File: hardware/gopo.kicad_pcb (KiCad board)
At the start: 4 copper layers, 65.9 x 40.6 mm, 99 parts, among them J2 DS1021-1X3SF11-B, J3 NHD-2.4-240320AF-CSXP, J4 DG142R-5.08-02P-14-00AH, J7 USB_C_Receptacle_USB2.0_16P, Q1 BSS138, Q2 BSS138, Q3 IRF7855TRPBF, Q4 IRF7855TRPBF, SW1 BOOT / PTS810, SW2 RESET / PTS810, SW3 L-KLS4-EC1121S-E5A-F12.5, U1 AP33772SDKZ-13-FA02, U10 TPD4EUSB30, U2 ESP32-C6-WROOM-1, U3 INA228, U4 RV-3028-C7, U5 AOZ1284PI, U6 TL431BIDBZR, U7 TPS61023DRLR, U8 CAT4104V-GT3, U9 TPD4E05U06QDQARQ1

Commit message: hardware: RTC'yi BQ32000 + süper kapasitöre geçir, Özdisan BOM'unu şemaya aktar
RTC (mcu):
- U4 RV-3028-C7 -> BQ32000DR (SOIC-8, I2C 0x68, open-drain IRQ, dahili
  trickle charger). Y1 ABS25-32.768KHZ-T (CL 12,5 pF, harici yük C yok),
  C33 Korchip DCL5R5155HF 1,5 F/5,5 V (H-tipi yatay coin, ~22 gün yedek).
- BT1 (CR2032), R22, R23, C10 kaldırıldı; C9 100n -> 1u0 (datasheet >= 1 uF).
- Yeni footprint: Power_Output_Custom:Korchip_DCL_H-Type_D19.0mm_P20.00mm_Horizontal
  (Korchip DCL datasheet çiziminden; numune ile doğrulanmalı).
- Beklenen netlist farkı yalnız RTC netleri: RTC_SCL/SDA/INT U4 pin
  numaraları, Net-(U4-OSCI/OSCO/VBACK) yeni; Net-(BT1-+), Net-(U4-EVI),
  Net-(U4-VBACKUP), U4 CLKOUT kalktı. ERC değişmedi (0 hata, 2 eski uyarı).

Özdisan BOM aktarımı (tüm sayfalar):
- MPN, Manufacturer, parametrik alanlar ve SelectionNote (Özdisan kodu,
  stok 21.09.2026, durum) BOM_OZDISAN_REV_C_20260921.xlsx'ten yazıldı.
- Onaylı değişiklikler: C5/C20/C21 0805; C8/C12/C13/C25/C27/C28 4u7 50V
  X7R 1210; C15/C29 47u 35V hibrit (Device:C_Polarized, CP_Elec_6.3x5.8);
  C31 0603 25V; R59 0805 1/3W; R40 3k24 + R39 10k2 (VOUT 3,3185 V);
  U6 TL431AIDBZR; D4 SX36.
- Stokta olmayan parçalarda (U1, U2, U7, U8, U10, U12, L1, L2, C19) MPN
  korundu, öneri SelectionNote ve todo.txt'de. Alan geometrisi ve
  görünürlük değişmedi. PCB şemadan henüz güncellenmedi.

Aynı commit'te önceden commit edilmemiş çalışma: Q3/Q5 SQJB60EP ve U3
INA226 entegrasyonu, raporları ve datasheet'leri.

Co-Authored-By: Claude Opus 5 <noreply@anthropic.com>
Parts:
- U3: value INA228 -> INA226
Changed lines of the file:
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@@
 			)
 		)
-		(property "Value" "INA228"
+		(property "Value" "INA226"
 			(at 0 -2.45 90)
 			(layer "B.Fab")
@@
 			)
 		)
-		(property "MPN" "INA228AIDGSR"
+		(property "MPN" "INA226AIDGSR"
 			(at 0 0 270)
 			(unlocked yes)

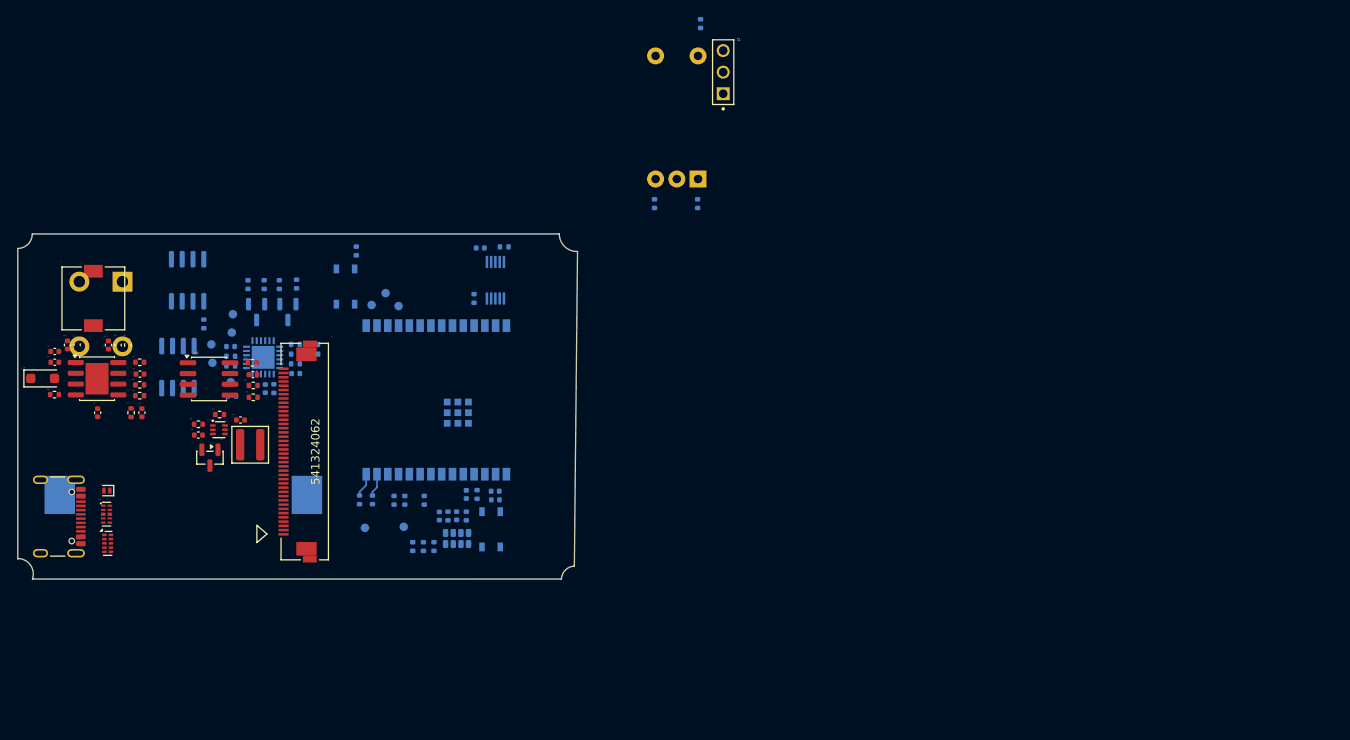
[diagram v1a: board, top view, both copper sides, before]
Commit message: hardware: PCB'yi şemadan güncelle (TASK-006)
54 footprint eklendi, 15 kaldırıldı, 20 footprint değişti; alanlar ve
netler şemayla eşitlendi, eski WROOM-1/BT1 pad'lerine giden 7 iz
parçası silindi. DRC schematic parity 416 -> 1 (J8, footprint TBD).
kicad-schematic skill'ine headless update_pcb.py eklendi.

Co-Authored-By: Claude Opus 5.5 <noreply@anthropic.com>
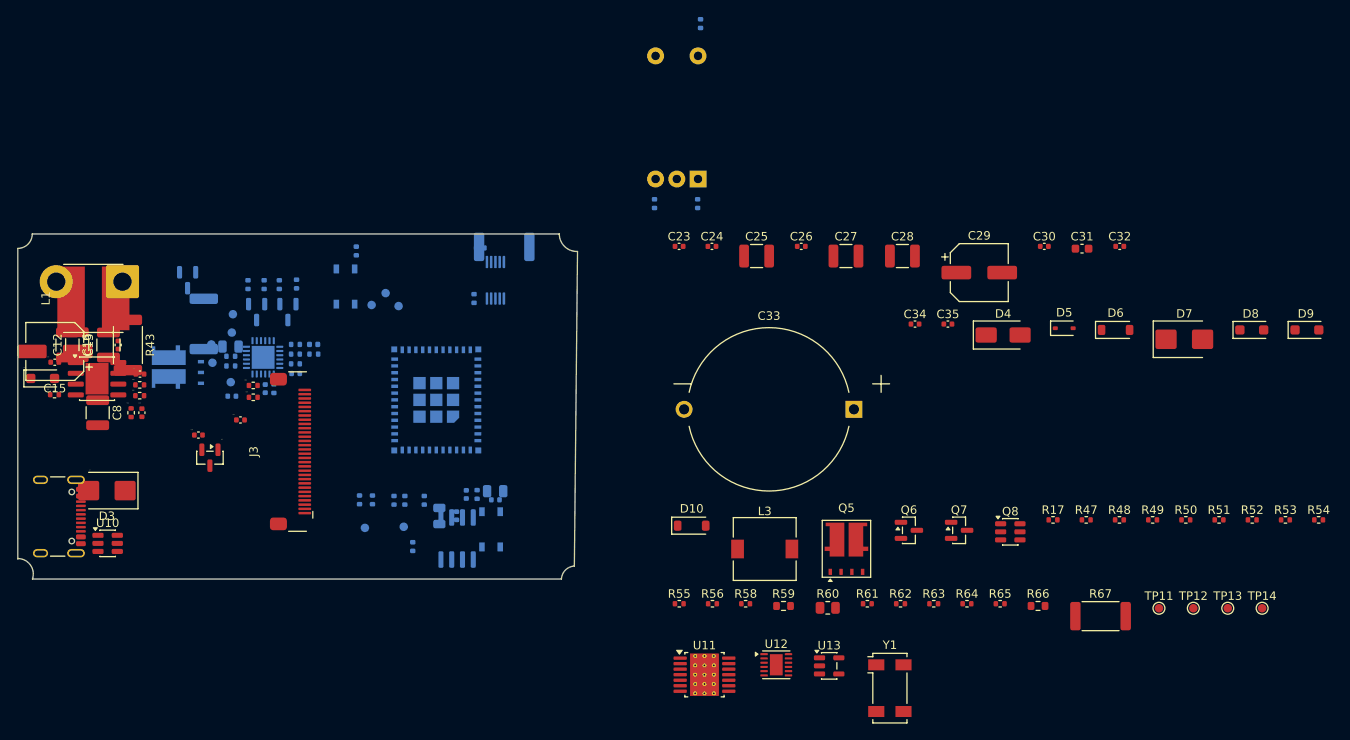
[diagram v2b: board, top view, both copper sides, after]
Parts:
- removed BT1: CR2032 holder, Power_Output_Custom:KLS_CR2032_05
- removed C22: 100nF / 16V, Capacitor_SMD:C_0402_1005Metric
- removed J2: DS1021-1X3SF11-B, CONNFLY_DS1021-1X3SF11-B:CONNFLY_DS1021-1X3SF11-B
- removed L2: 2.2uH, Inductor_SMD:L_Wuerth_MAPI-4030
- removed R22: 1K, Resistor_SMD:R_0402_1005Metric
- removed R23: 10k, Resistor_SMD:R_0402_1005Metric
- removed R25: 4.7k, Resistor_SMD:R_0402_1005Metric
- removed R26: 4.7K, Resistor_SMD:R_0402_1005Metric
- removed R42: 100kR, Resistor_SMD:R_0402_1005Metric
- removed R44: 604kR 0.1%, Resistor_SMD:R_0402_1005Metric
- removed R45: 100kR 0.1%, Resistor_SMD:R_0402_1005Metric
- removed R46: 3.24kR 0.1%, Resistor_SMD:R_0402_1005Metric
- removed U7: TPS61023DRLR, Power_Management_Custom:TPS61023_DRL0006A
- removed U8: CAT4104V-GT3, Package_SO:SOIC-8_3.9x4.9mm_P1.27mm
- removed U9: TPD4E05U06QDQARQ1, USB_ESD:antmicro_tpd4e05u06qdqarq1
- added C23: 47n, Capacitor_SMD:C_0402_1005Metric, F.Cu at (102.4, 89.9)
- added C24: 100n, Capacitor_SMD:C_0402_1005Metric, F.Cu at (106.2, 89.9)
- added C25: 4u7, Capacitor_SMD:C_1210_3225Metric, F.Cu at (111.5, 91.0)
- added C26: 100n, Capacitor_SMD:C_0402_1005Metric, F.Cu at (116.8, 89.9)
- added C27: 4u7, Capacitor_SMD:C_1210_3225Metric, F.Cu at (122.0, 91.0)
- added C28: 4u7, Capacitor_SMD:C_1210_3225Metric, F.Cu at (128.7, 91.0)
- added C29: 47u, Capacitor_SMD:CP_Elec_6.3x5.8, F.Cu at (137.7, 92.9)
- added C30: 22n, Capacitor_SMD:C_0402_1005Metric, F.Cu at (145.4, 89.9)
- added C31: 220n, Capacitor_SMD:C_0603_1608Metric, F.Cu at (149.8, 90.1)
- added C32: 100n, Capacitor_SMD:C_0402_1005Metric, F.Cu at (154.3, 89.9)
- added C33: 1F5, Power_Output_Custom:Korchip_DCL_H-Type_D19.0mm_P20.00mm_Horizontal, F.Cu at (123.0, 109.0)
- added C34: 1u0, Capacitor_SMD:C_0402_1005Metric, F.Cu at (130.2, 99.0)
- added C35: 100n, Capacitor_SMD:C_0402_1005Metric, F.Cu at (134.0, 99.0)
- added D10: BZT52C12, Diode_SMD:D_SOD-123, F.Cu at (103.9, 122.7)
- added D4: SX36, Diode_SMD:D_SMA, F.Cu at (140.5, 100.3)
- added D5: BAS16H, Diode_SMD:D_SOD-323, F.Cu at (147.7, 99.5)
- added D6: BZT52C12, Diode_SMD:D_SOD-123, F.Cu at (153.8, 99.7)
- added D7: SMBJ30A, Diode_SMD:D_SMB, F.Cu at (161.9, 100.8)
- added D8: SMF30A, Diode_SMD:D_SOD-123F, F.Cu at (169.8, 99.7)
- added D9: SMF30A, Diode_SMD:D_SOD-123F, F.Cu at (176.3, 99.7)
- added L3: 6u8, Inductor_SMD:L_7.3x7.3_H4.5, F.Cu at (112.5, 125.5)
- added Q5: SQJB60EP, Package_SO_Custom:Vishay_PowerPAK_SO-8L_Dual, F.Cu at (122.1, 125.5)
- added Q6: BSS138P, Package_TO_SOT_SMD:SOT-23, F.Cu at (129.4, 123.3)
- added Q7: IRLML6344, Package_TO_SOT_SMD:SOT-23, F.Cu at (135.4, 123.3)
- added Q8: TSM3443CX6, Package_TO_SOT_SMD:SOT-23-6, F.Cu at (141.4, 123.5)
- added R17: 100k, Resistor_SMD:R_0402_1005Metric, F.Cu at (146.4, 122.1)
- added R47: 78k7, Resistor_SMD:R_0402_1005Metric, F.Cu at (150.3, 122.1)
- added R48: 30k1, Resistor_SMD:R_0402_1005Metric, F.Cu at (154.2, 122.1)
- added R49: 9k76, Resistor_SMD:R_0402_1005Metric, F.Cu at (158.1, 122.1)
- added R50: 2k87, Resistor_SMD:R_0402_1005Metric, F.Cu at (162.1, 122.1)
- added R51: 9k76, Resistor_SMD:R_0402_1005Metric, F.Cu at (166.0, 122.1)
- added R52: 2k0, Resistor_SMD:R_0402_1005Metric, F.Cu at (169.9, 122.1)
- added R53: 100k, Resistor_SMD:R_0402_1005Metric, F.Cu at (173.8, 122.1)
- added R54: 1k0, Resistor_SMD:R_0402_1005Metric, F.Cu at (177.7, 122.1)
- added R55: 237k, Resistor_SMD:R_0402_1005Metric, F.Cu at (102.4, 131.9)
- added R56: 10k, Resistor_SMD:R_0402_1005Metric, F.Cu at (106.3, 131.9)
- added R58: 100k, Resistor_SMD:R_0402_1005Metric, F.Cu at (110.2, 131.9)
- added R59: 100k, Resistor_SMD:R_0603_1608Metric, F.Cu at (114.7, 132.2)
- added R60: 5R6, Resistor_SMD:R_0805_2012Metric, F.Cu at (119.9, 132.4)
- added R61: 4k7, Resistor_SMD:R_0402_1005Metric, F.Cu at (124.5, 131.9)
- added R62: 5k1, Resistor_SMD:R_0402_1005Metric, F.Cu at (128.5, 131.9)
- added R63: 5k1, Resistor_SMD:R_0402_1005Metric, F.Cu at (132.4, 131.9)
- added R64: 2k0, Resistor_SMD:R_0402_1005Metric, F.Cu at (136.3, 131.9)
- added R65: 10k, Resistor_SMD:R_0402_1005Metric, F.Cu at (140.2, 131.9)
- added R66: 100k, Resistor_SMD:R_0603_1608Metric, F.Cu at (144.6, 132.2)
- added R67: 1k, Resistor_SMD:R_2512_6332Metric, F.Cu at (152.0, 133.4)
- added TP11: TestPoint, TestPoint:TestPoint_Pad_D1.0mm, F.Cu at (158.9, 132.5)
- added TP12: TestPoint, TestPoint:TestPoint_Pad_D1.0mm, F.Cu at (162.9, 132.5)
- added TP13: TestPoint, TestPoint:TestPoint_Pad_D1.0mm, F.Cu at (167.0, 132.5)
- added TP14: TestPoint, TestPoint:TestPoint_Pad_D1.0mm, F.Cu at (171.0, 132.5)
- added U11: TPS55340PWPR, Package_SO:Texas_HTSSOP-14-1EP_4.4x5mm_P0.65mm_EP3.4x5mm_Mask3.155x3.255mm_ThermalVias, F.Cu at (105.4, 140.3)
- added U12: LM74801-Q1, Package_SON:WSON-12-1EP_3x3mm_P0.5mm_EP1.5x2.5mm, F.Cu at (113.8, 139.1)
- added U13: 74LVC1G08, Package_TO_SOT_SMD:SOT-23-5, F.Cu at (120.1, 139.3)
- added Y1: 32.768kHz, Crystal:Crystal_SMD_Abracon_ABS25-4Pin_8.0x3.8mm, F.Cu at (127.2, 141.9)
- C1, C2: value 100 nF -> 100n
- C10: value 100nF -> 22u; footprint Capacitor_SMD:C_0402_1005Metric -> Capacitor_SMD:C_0805_2012Metric
- C11, C14, C6: value 100nF -> 100n
- C12, C13: value 10uF -> 4u7; footprint Capacitor_SMD:C_0402_1005Metric -> Capacitor_SMD:C_1210_3225Metric
- C15: value 47uF -> 47u; footprint Capacitor_SMD:C_0402_1005Metric -> Capacitor_SMD:CP_Elec_6.3x5.8
- C16: value 47uF -> 47u; footprint Capacitor_SMD:C_0402_1005Metric -> Capacitor_SMD:C_1210_3225Metric
- C17: value 100nF / 16V -> 100n
- C18: value 10nF -> 10n
- C19: value 18nF / 16V -> 15n
- C20, C21: value 22uF -> 100n
- C3: value 1uF / 50V -> 2u2; footprint Capacitor_SMD:C_0402_1005Metric -> Capacitor_SMD:C_0805_2012Metric
- C4: value 1uF / 10V -> 1u0
- C5: value 22uF -> 22u; footprint Capacitor_SMD:C_0402_1005Metric -> Capacitor_SMD:C_0805_2012Metric
- C7: value 1uF -> 1u0
- C8: value 10uF / 50V -> 4u7; footprint Capacitor_SMD:C_0402_1005Metric -> Capacitor_SMD:C_1210_3225Metric
- C9: value 100nF -> 1u0
- D2: value SS2060FL_R1_00001 -> SS2060FL
- D3: value AQ3130E-01ETG (bidirectional) -> SMBJ30A; footprint Diode_SMD:D_SOD-882 -> Diode_SMD:D_SMB
- J3: value NHD-2.4-240320AF-CSXP -> TFT032B018; footprint Molex_541324062:CON_541324062_MOL -> Connector_FPC_Custom:KLS_L-KLS1-242I-2.0-30_1x30-2MP_P0.50mm_Horizontal
- J4: value DG142R-5.08-02P-14-00AH -> SolderWire-1.5sqmm; footprint DG142R-5.08-02P-14-00AH:DG142R-5.08-02P-14-00AH -> Connector_Wire:SolderWire-1.5sqmm_1x02_P7.8mm_D1.7mm_OD3.9mm
- L1: value SRI0704-220M -> 22u; footprint Inductor_SMD:L_7.3x7.3_H4.5 -> Inductor_Custom:L_CoreMaster_FPI0705_7.8x7.0mm_H5.0
- Q1, Q2: value BSS138 -> BSS138P
- Q3: value IRF7855TRPBF -> SQJB60EP; footprint Package_SO:SOIC-8_3.9x4.9mm_P1.27mm -> Package_SO_Custom:Vishay_PowerPAK_SO-8L_Dual
- Q4: value IRF7855TRPBF -> BSS138P; footprint Package_SO:SOIC-8_3.9x4.9mm_P1.27mm -> Package_TO_SOT_SMD:SOT-23
- R1: value 10 kΩ -> 10k
- R11, RShunt1: value 5mR / 1W -> 5m0; footprint Resistor_SMD:R_0402_1005Metric -> Resistor_SMD:R_2512_6332Metric
- R12: value 6.2k -> 6k2
- R14: value 2.2k -> 2k2
- R15: value 22 R -> 22R
- R16: value 22R -> 10k
- R2, R3: value 22Ω -> 22R
- R21: value 100K -> 100k
- R24: value 4,7k -> 4k7
- R27: value 10K -> 10k
- R29: value 100kR -> 100k
- R37: value 10kR -> 10k
- R38: value 100kR 1% -> 100k
- R39: value 10kR 0.1% -> 10k2
- R4: value 4.7 kΩ -> 4k7
- R40: value 3.20kR 0.1% -> 3k24
- R41: value 12.7kR 1% -> 51k
- R43: value 1kR / 2W -> 4k7; footprint Resistor_SMD:R_0402_1005Metric -> Resistor_SMD:R_2512_6332Metric
- R5: value 4.7kΩ -> 4k7
- R6: value 4.7 k -> 4k7
- R7: value 4.7k -> 4k7
- R8: value 12k -> 10k
- R9: value 20k -> 10k
- TH1: value TSM0B103F3381RZ / 10k NTC -> 10k NTC
- U10: value TPD4EUSB30 -> USBLC6-2SC6; footprint Package_SON:USON-10_2.5x1.0mm_P0.5mm -> Package_TO_SOT_SMD:SOT-23-6
- U2: value ESP32-C6-WROOM-1 -> ESP32-C6-MINI-1-H4; footprint PCM_Espressif:ESP32-C6-WROOM-1 -> RF_Module:ESP32-C6-MINI-1
- U4: value RV-3028-C7 -> BQ32000; footprint Package_SON:MicroCrystal_C7_SON-8_1.5x3.2mm_P0.9mm -> Package_SO:SOIC-8_3.9x4.9mm_P1.27mm
- U6: value TL431BIDBZR -> TLV431BQDBZT
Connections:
- net /POWER GENERATION/COMP_NODE renamed /USB_PD_CONTROLLER/COMP_NODE
- net /POWER GENERATION/FB_3V3 renamed /USB_PD_CONTROLLER/FB_3V3
- net /POWER GENERATION/FSW_SET renamed /USB_PD_CONTROLLER/FSW_SET
- net /POWER GENERATION/LX_SW renamed /USB_PD_CONTROLLER/LX_SW
- net /POWER GENERATION/SS_RAMP renamed /USB_PD_CONTROLLER/SS_RAMP
- net Net-(R15-Pad2) renamed /MCU/ETH_CFG0
- C10 pad 1: Net-(U4-VBACKUP) -> /MCU/ETH_3V3
- C12 pad 1: PD_VOUT -> V_PRE
- C13 pad 1: PD_VOUT -> V_PRE
- C14 pad 1: PD_VOUT -> V_PRE
- C20 pad 1: +3.3V -> /MCU/ETH_3V3
- C21 pad 1: BACKLIGHT_4V2 -> +3.3V
- C21 pad 2: GND -> /MCU/ETH_PWR_EN
- C3 pad 1: PD_VBUS_SENSED -> /USB_PD_CONTROLLER/PD_VBUS_SENSED
- C7 pad 2: Net-(U2-EN/CHIP_PU) -> Net-(U2-EN)
- D3 pad 1: GND -> USB_VBUS
- D3 pad 2: USB_VBUS -> GND
- J3 pad 1: GND -> unconnected-(J3-Pin_1-Pad1)
- J3 pad 10: TFT_CS -> GND
- J3 pad 11: TFT_SCLK -> GND
- J3 pad 12: TFT_DC -> GND
- J3 pad 16: GND -> TFT_DC
- J3 pad 17: GND -> TFT_SCLK
- J3 pad 18: GND -> TFT_CS
- J3 pad 19: GND -> TFT_MOSI
- J3 pad 2: unconnected-(J3-Pin_2-Pad2) -> /USER INTERFACE/BL_A
- J3 pad 20: GND -> TFT_RST
- J3 pad 21: GND -> +3.3V
- J3 pad 22: GND -> +3.3V
- J3 pad 23: GND -> +3.3V
- J3 pad 24: GND -> unconnected-(J3-Pin_24-Pad24)
- J3 pad 26: GND -> unconnected-(J3-Pin_26-Pad26)
- J3 pad 27: GND -> unconnected-(J3-Pin_27-Pad27)
- J3 pad 28: GND -> unconnected-(J3-Pin_28-Pad28)
- J3 pad 29: GND -> unconnected-(J3-Pin_29-Pad29)
- J3 pad 30: TFT_RST -> GND
- J3 pad 4: unconnected-(J3-Pin_4-Pad4) -> /USER INTERFACE/BL_K
- J3 pad 5: unconnected-(J3-Pin_5-Pad5) -> GND
- J3 pad 7: +3.3V -> GND
- J3 pad 8: +3.3V -> GND
- J3 pad 9: TFT_MOSI -> GND
- Q3 pad 1: Net-(Q3-S-Pad1) -> Net-(Q3A-S)
- Q3 pad 2: Net-(Q3-S-Pad1) -> /USB_PD_CONTROLLER/PD_GATE
- Q3 pad 3: Net-(Q3-S-Pad1) -> Net-(Q3A-S)
- Q3 pad 7: PD_VOUT -> /USB_PD_CONTROLLER/PD_VBUS_SENSED
- Q3 pad 8: PD_VOUT -> /USB_PD_CONTROLLER/PD_VBUS_SENSED
- Q4 pad 1: Net-(Q3-S-Pad1) -> /USB_PD_CONTROLLER/SW_EN
- Q4 pad 2: Net-(Q3-S-Pad1) -> GND
- Q4 pad 3: Net-(Q3-S-Pad1) -> /USB_PD_CONTROLLER/DISCH_G
- R1 pad 2: Net-(U2-EN/CHIP_PU) -> Net-(U2-EN)
- R10 pad 1: Net-(U2-GPIO9) -> Net-(U2-IO9)
- R11 pad 2: PD_VBUS_SENSED -> /USB_PD_CONTROLLER/PD_VBUS_SENSED
- R15 pad 1: Net-(U2-GPIO8) -> Net-(U2-IO8)
- R16 pad 1: Net-(R16-Pad1) -> /MCU/ETH_PWR_EN
- R16 pad 2: Net-(U2-GPIO0/ADC1_CH0/XTAL_32K_P) -> Net-(U2-IO0)
- R2 pad 1: Net-(U2-GPIO13/USB_D+) -> Net-(U2-IO12)
- R2 pad 2: USB_DP -> USB_DM
- R3 pad 1: Net-(U2-GPIO12/USB_D-) -> Net-(U2-IO13)
- R3 pad 2: USB_DM -> USB_DP
- R37 pad 1: +3.3V -> Net-(U2-IO8)
- R37 pad 2: Net-(U2-GPIO8) -> +3.3V
- R43 pad 1: PD_VOUT -> V_PRE
- R43 pad 2: /POWER GENERATION/EN_CTRL -> /USB_PD_CONTROLLER/EN_CTRL
- R8 pad 2: PD_INT_3V3 -> Net-(R64-Pad1)
- R9 pad 2: GND -> Net-(R65-Pad1)
- RShunt1 pad 1: PD_VOUT -> /USB_PD_CONTROLLER/SW_OUT
- SW1 pad 2: Net-(U2-GPIO9) -> Net-(U2-IO9)
- SW2 pad 2: Net-(U2-EN/CHIP_PU) -> Net-(U2-EN)
- TP10 pad 1: Net-(R16-Pad1) -> /MCU/ETH_PWR_EN
- TP2 pad 1: PD_VBUS_SENSED -> /USB_PD_CONTROLLER/PD_VBUS_SENSED
- U1 pad 24: PD_VBUS_SENSED -> /USB_PD_CONTROLLER/PD_VBUS_SENSED
- U10 pad 1: unconnected-(U10-D1+-Pad1) -> USB_DM
- U10 pad 2: unconnected-(U10-D1--Pad2) -> GND
- U10 pad 3: Net-(U10-GND-Pad3) -> USB_DP
- U10 pad 4: unconnected-(U10-D2+-Pad4) -> USB_DP
- U10 pad 5: unconnected-(U10-D2--Pad5) -> +3.3V
- U10 pad 6: unconnected-(U10-NC-Pad6) -> USB_DM
- U2 pad 10: Net-(U2-GPIO8) -> TFT_MOSI
- U2 pad 11: TFT_CS -> GND
- U2 pad 12: TFT_DC -> Net-(U2-IO0)
- U2 pad 13: Net-(U2-GPIO12/USB_D-) -> TFT_BL_PWM
- U2 pad 14: Net-(U2-GPIO13/USB_D+) -> GND
- U2 pad 15: Net-(U2-GPIO9) -> OUT_EN
- U2 pad 16: PD_I2C_SCL_3V3 -> TFT_DC
- U2 pad 17: PD_I2C_SDA_3V3 -> Net-(U2-IO12)
- U2 pad 18: PD_INT_3V3 -> Net-(U2-IO13)
- U2 pad 19: ENCODER_SW -> TFT_CS
- U2 pad 2: +3.3V -> GND
- U2 pad 20: ENCODER_A -> TFT_RST
- U2 pad 21: ENCODER_B -> unconnected-(U2-NC-Pad21)
- U2 pad 22: unconnected-(U2-NC-Pad22) -> Net-(U2-IO8)
- U2 pad 23: TFT_RST -> Net-(U2-IO9)
- U2 pad 24: /MCU/UART_RX -> PD_I2C_SCL_3V3
- U2 pad 25: /MCU/UART_TX -> PD_I2C_SDA_3V3
- U2 pad 26: INA_ALERT -> PD_INT_3V3
- U2 pad 27: /MCU/RTC_INT -> ENCODER_SW
- U2 pad 28: GND -> ENCODER_A
- U2 pad 29: GND -> ENCODER_B
- U2 pad 3: Net-(U2-EN/CHIP_PU) -> +3.3V
- U2 pad 4: TFT_SCLK -> unconnected-(U2-NC-Pad4)
- U2 pad 5: TFT_MOSI -> /MCU/RTC_INT
- U2 pad 6: /MCU/RTC_SDA -> INA_ALERT
- U2 pad 7: /MCU/RTC_SCL -> unconnected-(U2-NC-Pad7)
- U2 pad 8: Net-(U2-GPIO0/ADC1_CH0/XTAL_32K_P) -> Net-(U2-EN)
- U2 pad 9: TFT_BL_PWM -> TFT_SCLK
- U3 pad 10: PD_VOUT -> /USB_PD_CONTROLLER/SW_OUT
- U4 pad 1: unconnected-(U4-CLKOUT-Pad1) -> Net-(U4-OSCI)
- U4 pad 2: /MCU/RTC_INT -> Net-(U4-OSCO)
- U4 pad 3: /MCU/RTC_SCL -> Net-(U4-VBACK)
- U4 pad 4: /MCU/RTC_SDA -> GND
- U4 pad 5: GND -> PD_I2C_SDA_3V3
- U4 pad 6: Net-(U4-VBACKUP) -> PD_I2C_SCL_3V3
- U4 pad 7: +3.3V -> /MCU/RTC_INT
- U4 pad 8: Net-(U4-EVI) -> +3.3V
- U5 pad 8: /POWER GENERATION/EN_CTRL -> /USB_PD_CONTROLLER/EN_CTRL
- U5 pad 9: PD_VOUT -> V_PRE
- U6 pad 1: /POWER GENERATION/EN_CTRL -> Net-(U6-REF)
- U6 pad 2: /POWER GENERATION/EN_CTRL -> /USB_PD_CONTROLLER/EN_CTRL
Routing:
- net Net-(U2-GPIO13/USB_D+): track 2.83 -> 0.00 mm
- net Net-(U2-GPIO12/USB_D-): track 2.73 -> 0.00 mm
- net Net-(BT1-+): track 0.72 -> 0.00 mm

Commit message: hardware: J8 Ethernet modulu footprint'i, 3D model ve PCB (TASK-054)
- Yeni kutuphane Module_Custom (fp-lib-table): Waveshare_2-CH_UART_TO_ETH.
  Standoff yok, 2x8 2.54 mm header + RJ45 tarafinda iki mekanik pin (MP,
  net yok) ile dogrudan lehim; RJ45 pim alaninda F.Cu keepout; courtyard
  RJ45'in 4.3 mm tasmasini kapsar. Olculer Waveshare olcu cizimi ve modul
  semasindan; mekanik pin konumu numuneyle dogrulanacak (TASK-053).
- Module_Custom.3dshapes: basitlestirilmis STEP (uretici model yayinlamiyor).
  Kaynak: .claude/skills/kicad-footprint/examples/waveshare_2ch_uart_to_eth.py
- mcu: J8 Footprint atandi, Value TBD -> 2-CH UART TO ETH, Manufacturer/
  Pitch/Height/SelectionNote (SAMM MP02965)/AssemblyNote. Netlist degismedi,
  ERC 0/0.
- PCB: J8 eklendi (update_pcb --keep-tracks), 3D model bagli; DRC schematic
  parity 1 -> 0. pcbnew kaydi karttaki metinlere (thickness ...) ekledi
  (~2500 satir, bicim normalizasyonu, baglanti degisikligi yok).
- CHANGES.TXT guncellendi.

Co-Authored-By: Claude Opus 5.5 <noreply@anthropic.com>
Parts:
- added J8: 2-CH UART TO ETH, Module_Custom:Waveshare_2-CH_UART_TO_ETH, F.Cu at (157.2, 109.5)
